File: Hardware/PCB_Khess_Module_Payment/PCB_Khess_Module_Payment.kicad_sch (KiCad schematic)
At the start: 22 parts, among them J3 Conn_01x08, J4 Conn_01x04, J6 Conn_01x08, U1 RASPBERRY_PI_ZERO_2_W

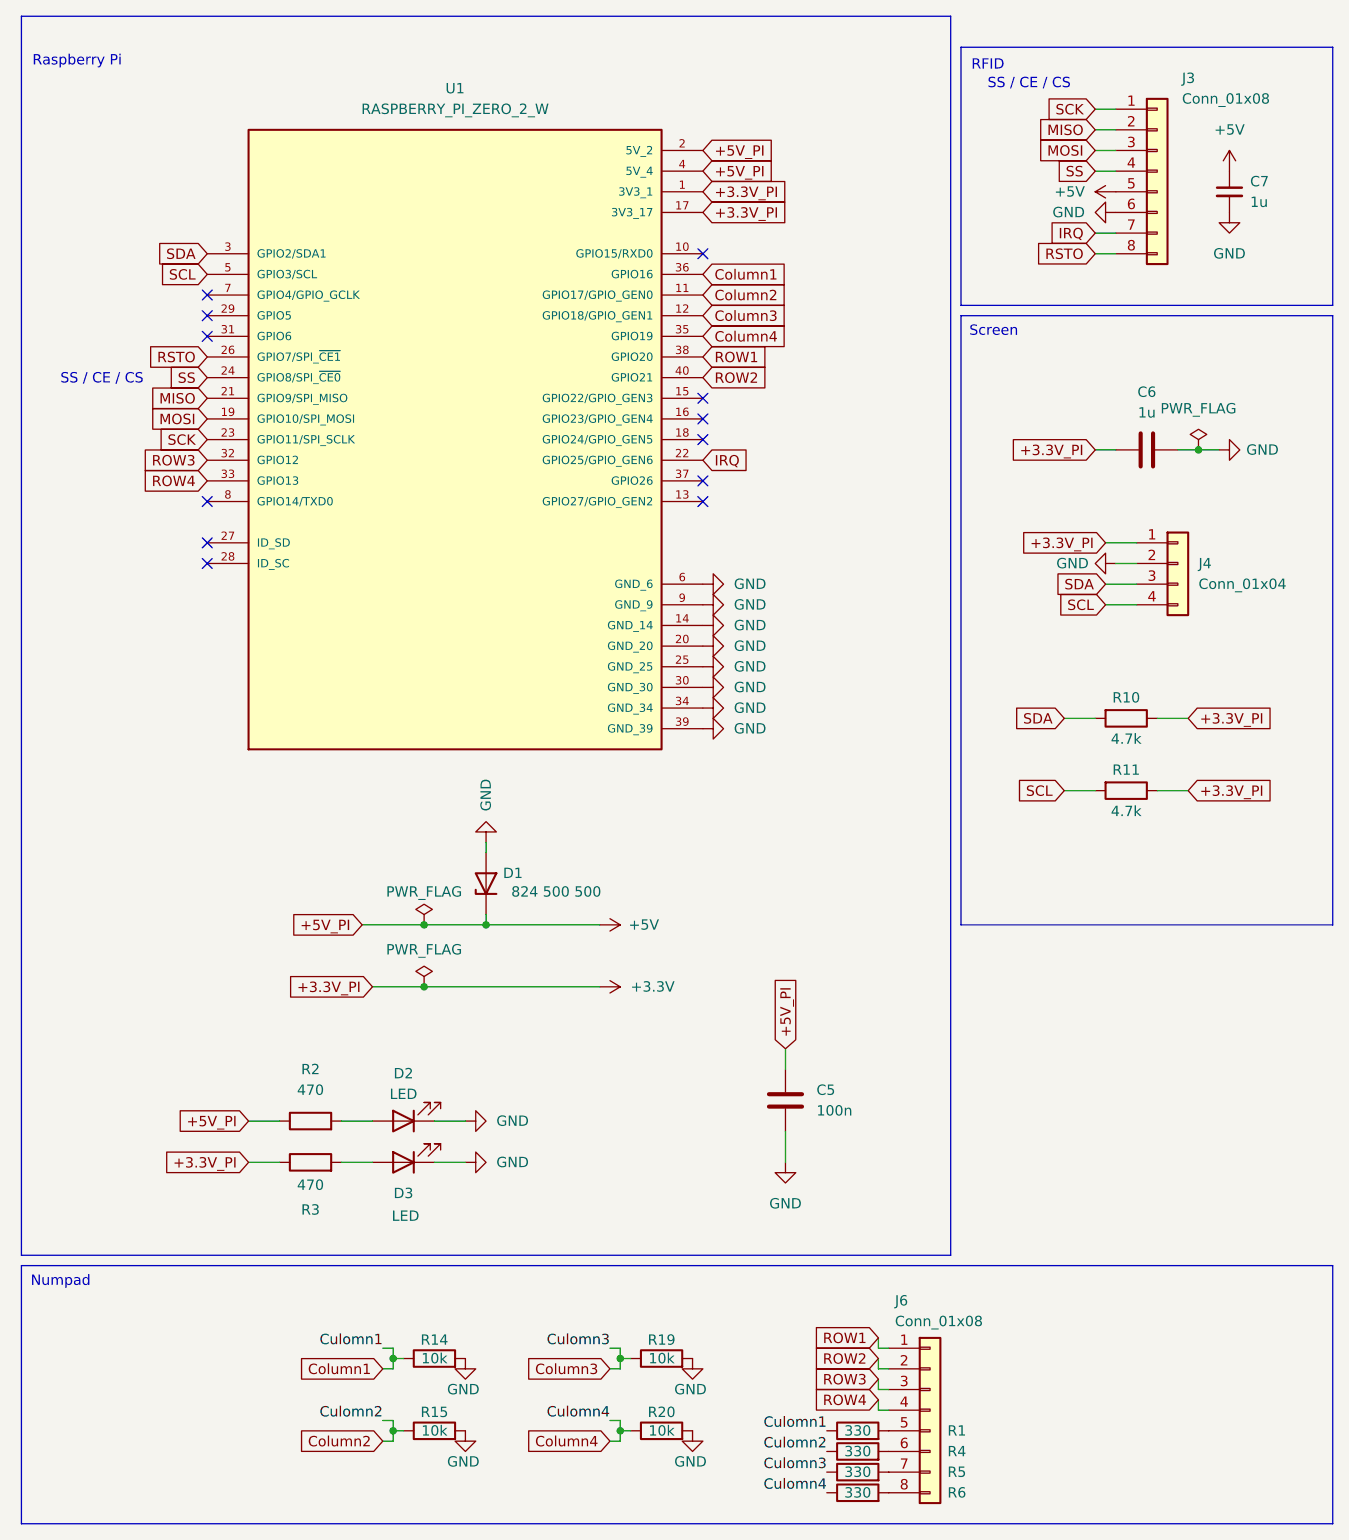
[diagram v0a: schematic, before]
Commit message: fix: update two pcb and add gnd via
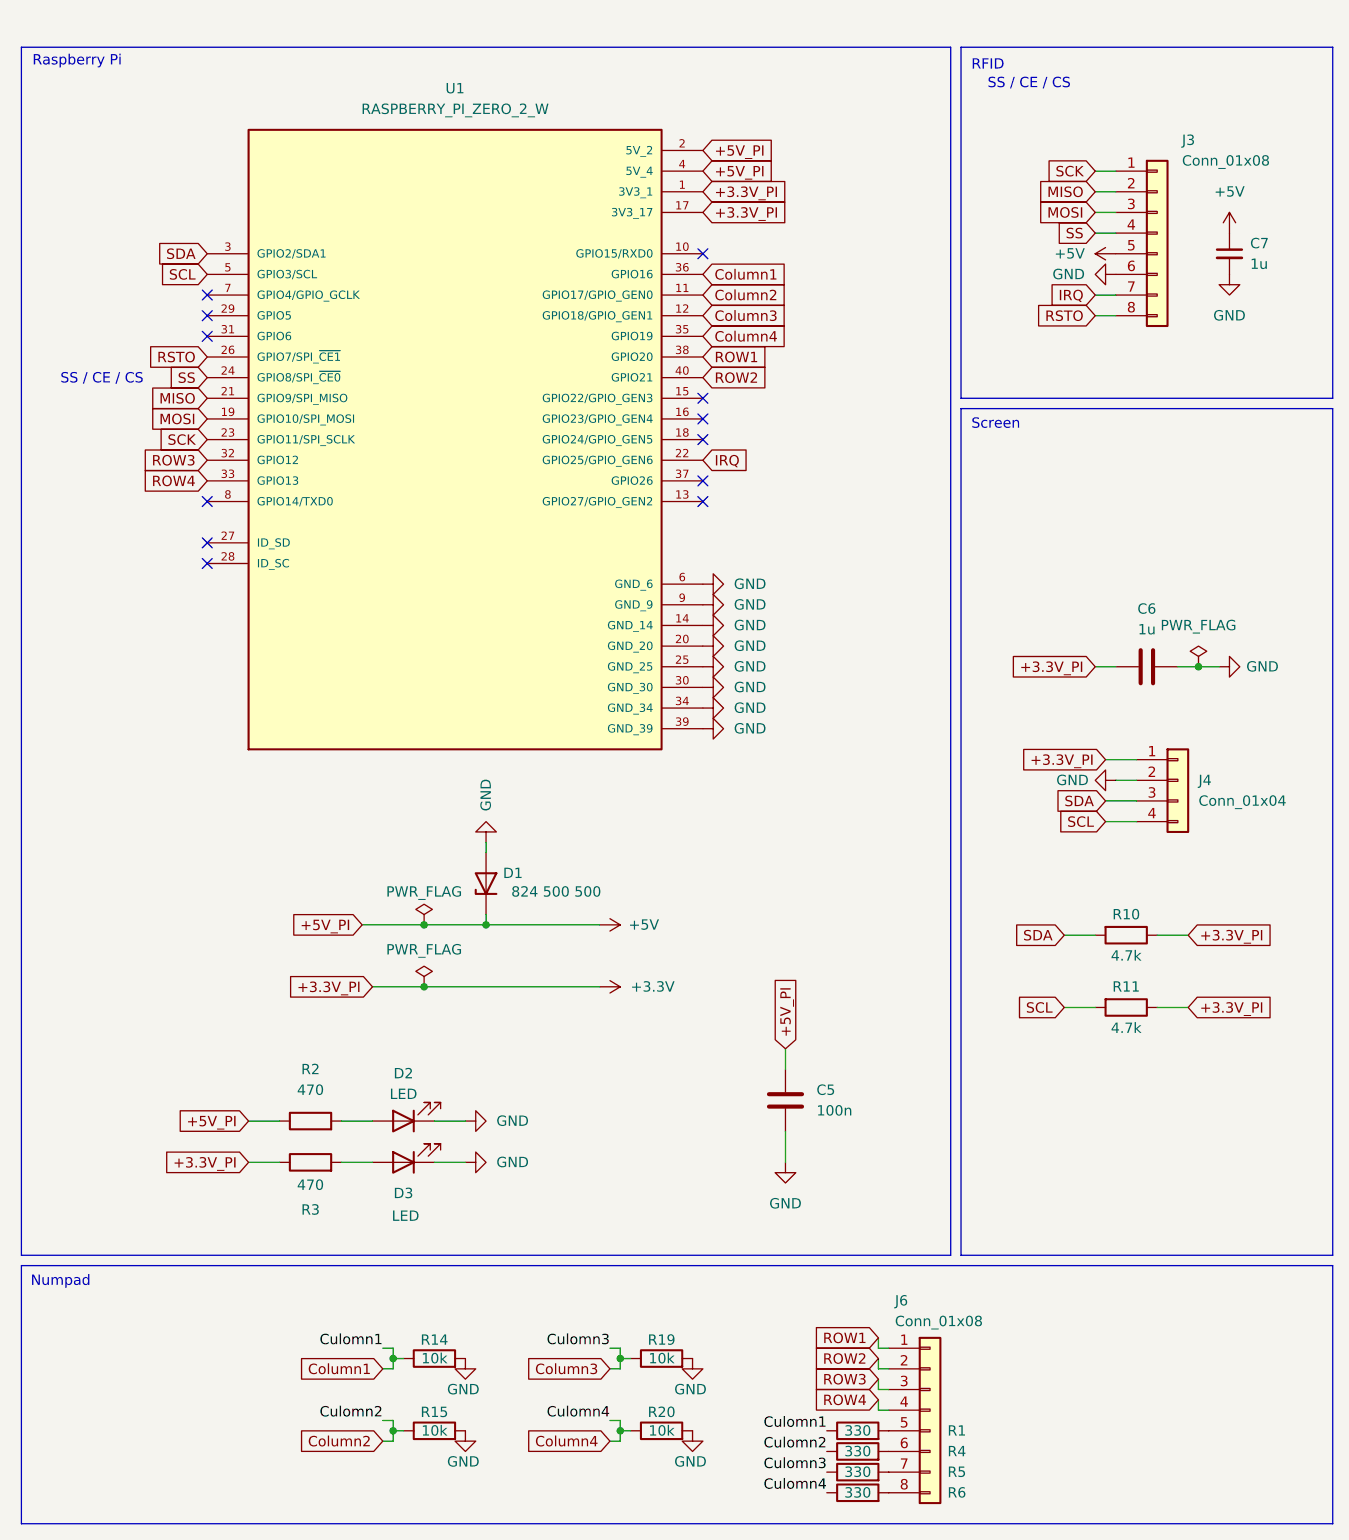
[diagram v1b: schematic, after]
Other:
- moved on the sheet: C6, C7, J3, J4, R10, R11

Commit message: fix
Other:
- company: (none) -> ENSEA
- title: (none) -> PCB Khess Module Payment
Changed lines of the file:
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@@
 	(generator_version "9.0")
 	(paper "A4")
+	(title_block
+		(title "PCB Khess Module Payment")
+		(date "2026-05-19")
+		(rev "1.0")
+		(company "ENSEA")
+		(comment 1 "Bryan-Sowanna Ing / Naïm Kirmat / Margaux Laplante / Rayan Laghouane")
+		(comment 2 "Estelle Zhang / Clément Jouneau / Rim Bouchikhi")
+	)
 	(rectangle
 		(start 129.54 58.42)
